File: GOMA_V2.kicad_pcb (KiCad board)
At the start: 2 copper layers, 81.3 x 104.1 mm, 90 parts, among them J1 ch1 in, J10 ch3 in, J11 ch3 out, J12 Conn_01x07_Pin, J13 Conn_01x07_Socket, J14 ch4 in, J15 ch4 out, J16 Conn_01x08_Pin, J17 Conn_01x08_Socket, J18 Conn_02x05_Odd_Even, J19 Daisy out, J2 ch1 out, J3 Daisy in, J4 ch2 in, J5 ch2 out, J6 Conn_01x07_Pin, J7 Conn_01x07_Socket, J8 Conn_01x07_Pin, J9 Conn_01x07_Socket, SW1 SW_SPST, SW2 SW_SPST, SW3 SW_SPST, SW4 SW_SPST, U1 LM324, U2 LM324, U3 LM324, U4 LM324, U6 LM78L05_TO92

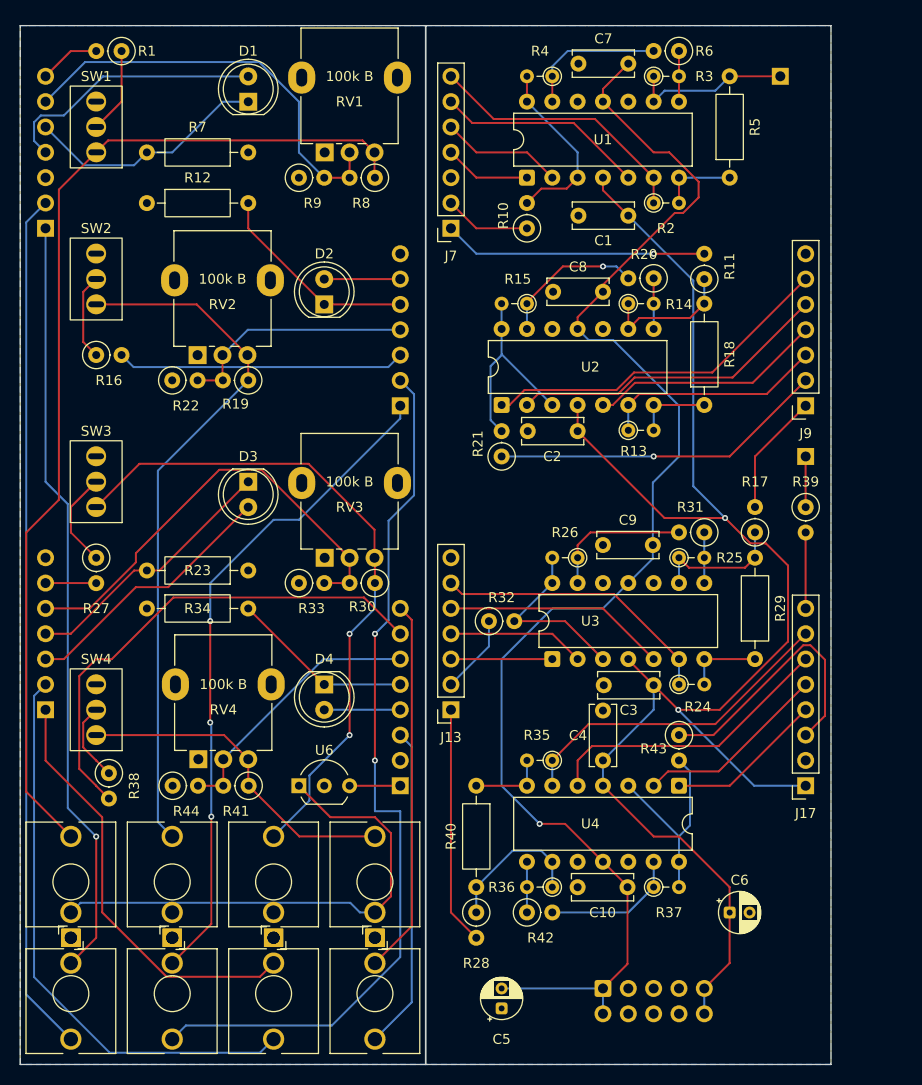
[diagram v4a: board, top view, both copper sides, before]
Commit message: adjusted component positioning
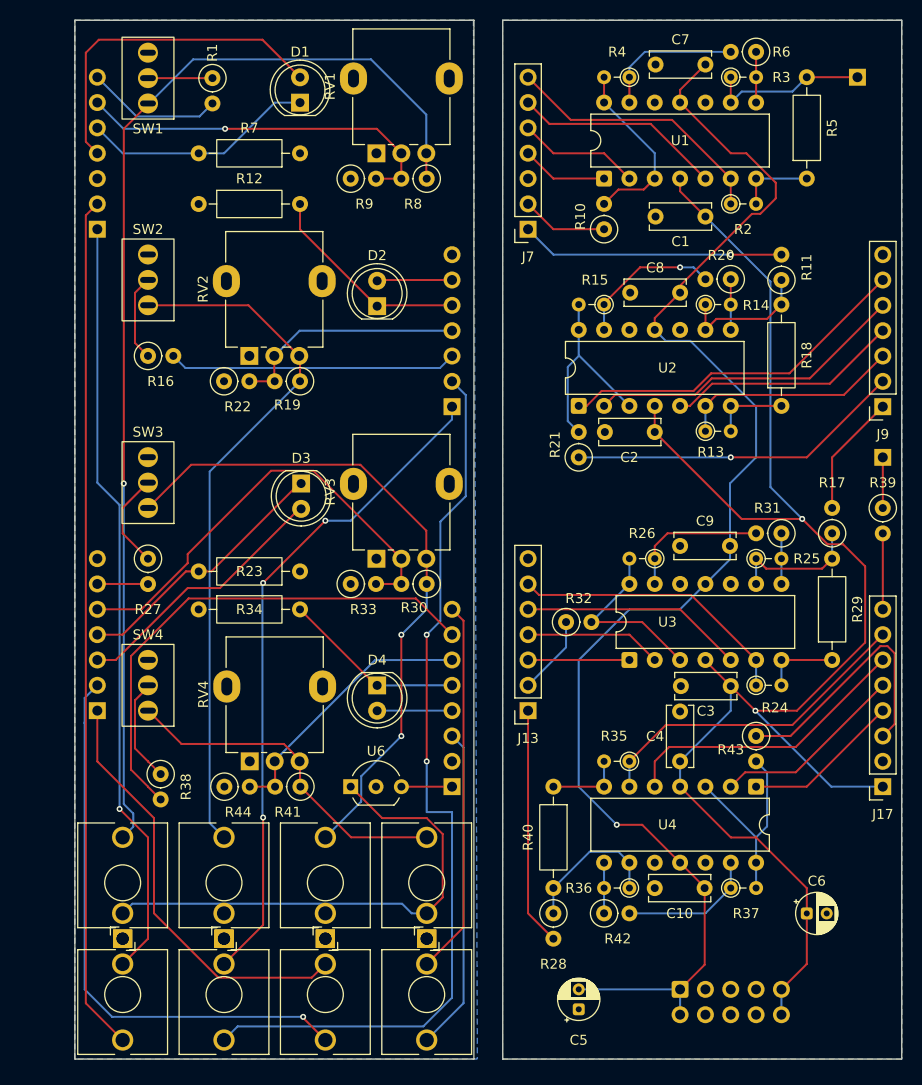
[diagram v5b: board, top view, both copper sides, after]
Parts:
- RV1, RV2, RV3, RV4: footprint Potentiometer_THT:Potentiometer_Alpha_RD901F-40-00D_Single_Vertical -> Custom:Potentiometer_Alpha_RD901F-40-00D_Single_Vertical_3D
- moved R1 9.51 mm to (85.2, 86.5), turned to -90 degrees
- moved J3 7.73 mm to (149.9, 86.4)
- moved R11 7.73 mm to (142.2, 106.7)
- moved R18 7.73 mm to (142.2, 119.3)
- moved R31 7.73 mm to (142.2, 132.1)
- moved C1 7.73 mm to (134.6, 100.3)
- moved C4 7.73 mm to (132.1, 154.9)
- moved C5 7.73 mm to (121.9, 179.8)
- moved C7 7.73 mm to (129.6, 85.1)
- moved C9 7.73 mm to (132.1, 133.3)
- moved J13 7.73 mm to (116.8, 149.9)
- moved J18 7.73 mm to (132.1, 177.8)
- moved J7 7.73 mm to (116.8, 101.6)
- moved R13 7.73 mm to (134.6, 121.8)
- moved R14 7.73 mm to (134.6, 109.2)
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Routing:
- net Net-(SW1-A): track 104.7 -> 113.8 mm, vias 0 -> 1
- net U1.6_FP: track 6.13 -> 13.7 mm
- net U1.1_FP: track 26.9 -> 34.1 mm
- net U1.5_FP: track 42.4 -> 37.7 mm, vias 0 -> 1
- net Net-(SW4-B): track 7.96 -> 10.5 mm
- net R21_FP: track 88.8 -> 91.1 mm
- net Net-(SW1-B): track 8.66 -> 6.35 mm
- net U4.6_FP: track 50.5 -> 51.7 mm
- net U1.2_FP: track 24.5 -> 23.5 mm
- net Net-(SW4-A): track 33.6 -> 34.5 mm
- net R10_FP: track 86.5 -> 85.8 mm
- net R43_BP: track 27.3 -> 26.7 mm
- net R32_FP: track 57.5 -> 57.4 mm, vias 0 -> 1
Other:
- board size 81.3 x 104.1 mm -> 82.9 x 104.1 mm

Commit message: added fabrication silkscreen stuff, adjusted positionings
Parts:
- added G***: LOGO, LOGO, B.Cu at (143.7, 91.0)
- added REF**: Attenuverter_Panel, Custom:Attenuverter_Panel, F.Cu at (73.7, 77.5)
- C5, C6: moved to B.Cu
- moved D2 5.06 mm to (104.0, 104.8)
- moved D3 5.06 mm to (96.3, 122.6)
- moved D1 5.01 mm to (96.3, 84.5)
- moved D4 4.99 mm to (104.0, 142.9)
- moved SW1 3.97 mm to (81.0, 83.2)
- moved RV2 3.91 mm to (91.2, 111.1)
- moved SW3 3.91 mm to (81.0, 123.8)
- moved RV3 3.90 mm to (103.9, 131.4)
- moved RV1 3.90 mm to (103.9, 90.8)
- moved R15 3.89 mm to (126.7, 106.0)
- moved R34 3.89 mm to (86.1, 136.5)
- moved R42 3.89 mm to (126.7, 167.0)
- moved C10 3.89 mm to (131.8, 164.5)
- moved C2 3.89 mm to (131.8, 118.8)
- moved C3 3.89 mm to (139.4, 144.2)
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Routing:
- net U3.5_FP: track 45.5 -> 39.8 mm, vias 0 -> 1
- net U2.2_FP: track 20.9 -> 20.1 mm
- net Net-(SW1-A): track 113.8 -> 114.5 mm
- net U3.1_FP: track 26.6 -> 27.3 mm
- net U3.2_FP: track 26.6 -> 27.3 mm
- net Net-(SW3-A): track 67.3 -> 68.0 mm
- net U4.5_FP: track 27.1 -> 27.7 mm
- net U1.2_FP: track 23.5 -> 24.0 mm
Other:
- board text added: "-12V stripe"
- board text added: "Daisy chain In"
- board text added: "Daisy chain Out"
- board text added: "JLCJLCJLCJLC"
- board text added: "Switchable Cascading Attenu-ator/-verter With 5V offset github.com/gunida v3 2025-08"
- board text added: "This one faces the other way!"
- board text added: "This side intent- ionally left blank"

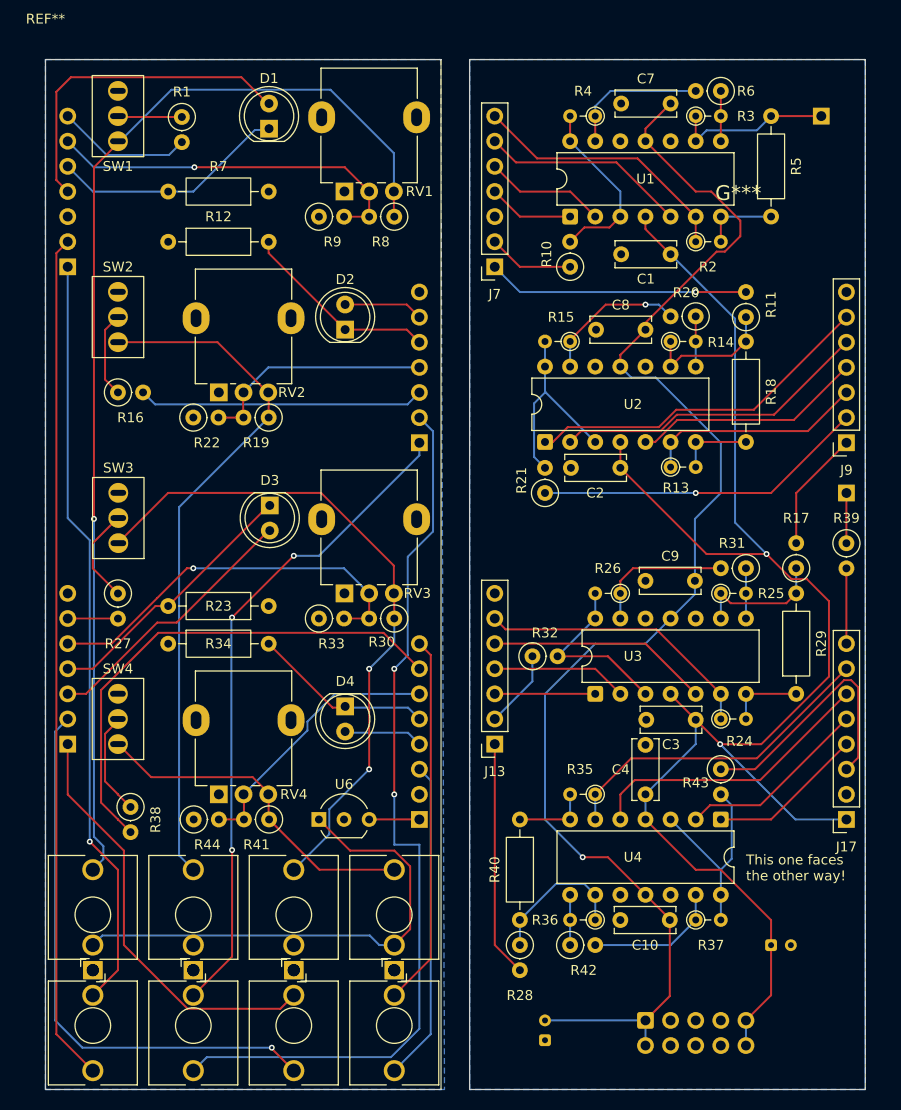
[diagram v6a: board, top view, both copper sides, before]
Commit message: Added voltage testpoints, front ground fill
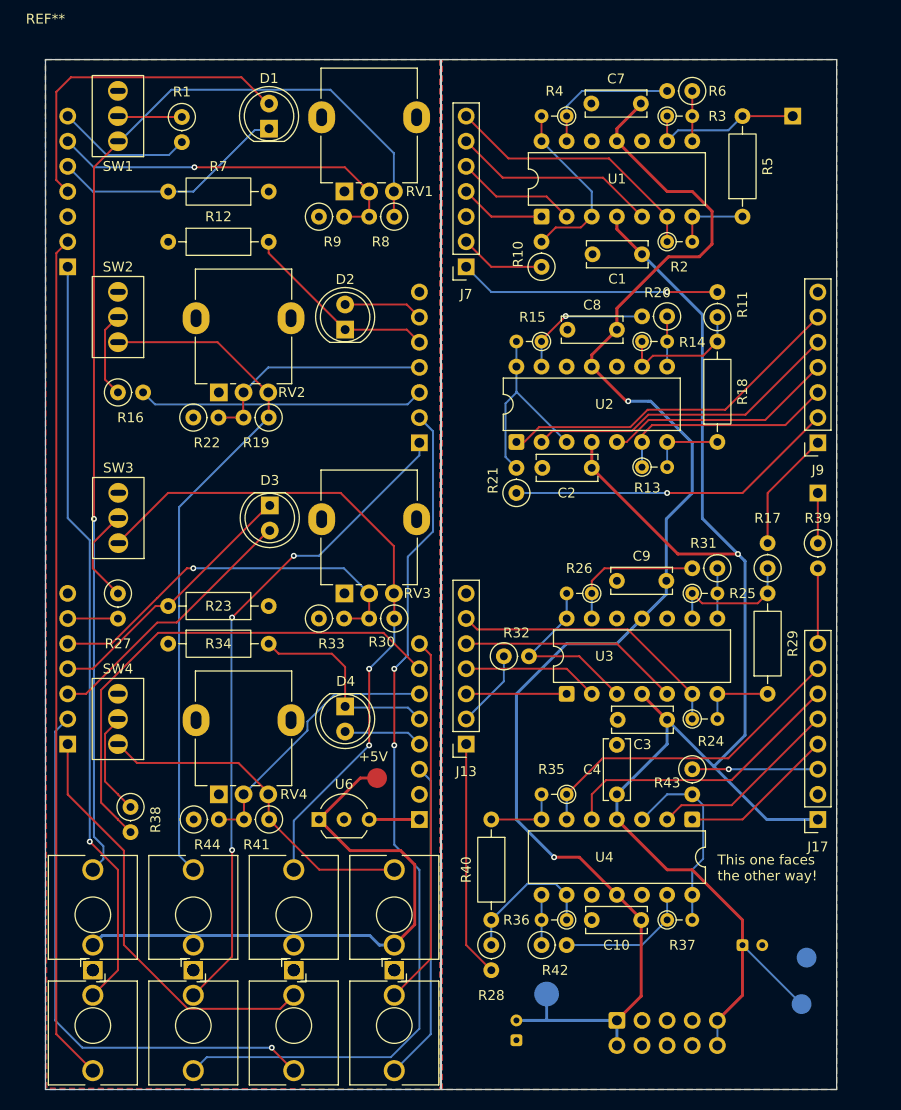
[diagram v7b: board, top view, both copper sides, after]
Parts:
- removed G***: LOGO, LOGO
- added TP1: GND, PCM_4ms_TestPoint:TestPoint_Pad_04, B.Cu at (150.6, 168.3)
- added TP2: +12V, PCM_4ms_TestPoint:TestPoint_Pad_04, B.Cu at (150.1, 173.0)
- added TP3: -12V, PCM_4ms_TestPoint:TestPoint_Pad_04, B.Cu at (124.3, 172.0)
- added TP4: +5V, PCM_4ms_TestPoint:TestPoint_Pad_04, F.Cu at (107.2, 150.1)
- moved C7 3.01 mm to (128.9, 81.9)
- moved C8 2.89 mm to (126.4, 104.8)
- moved R10 2.89 mm to (123.8, 98.4)
- moved R15 2.89 mm to (123.8, 106.0)
- moved R42 2.89 mm to (123.8, 167.0)
- moved U1 2.89 mm to (123.8, 93.3)
- moved C1 2.89 mm to (134.0, 97.2)
- moved C10 2.89 mm to (128.9, 164.5)
- moved C2 2.89 mm to (128.9, 118.8)
- moved C3 2.89 mm to (136.5, 144.2)
- moved C4 2.89 mm to (131.4, 151.8)
- moved C5 2.89 mm to (121.3, 176.6)
- moved C6 2.89 mm to (144.1, 167.0)
- moved C9 2.89 mm to (131.4, 130.2)
- moved J13 2.89 mm to (116.2, 146.7)
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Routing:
- net R43_BP: track 26.7 -> 12.7 mm, vias 0 -> 1
- net +5V_FP: track 51.1 -> 59.5 mm
- net -12V: track 139.8 -> 143.7 mm, vias 1 -> 2
- net U4.2_FP: track 18.4 -> 20.8 mm
- net +12V: track 155.8 -> 157.8 mm, vias 2 -> 1
- net R21_FP: track 91.1 -> 89.7 mm
- net Net-(SW3-A): track 68.0 -> 69.1 mm
- net Net-(U4A-+): track 20.8 -> 19.7 mm
- net Net-(U2D--): track 14.7 -> 13.7 mm
- added copper zone on F.Cu, net GND
- added copper zone on F.Cu, net GND_FP
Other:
- board size 82.9 x 104.1 mm -> 80 x 104.1 mm
- board text added: "NC"
- board text added: "V-cut"
